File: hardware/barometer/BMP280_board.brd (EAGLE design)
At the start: 17.8 x 17.8 mm, 8 parts, among them U1 EM406FLAT

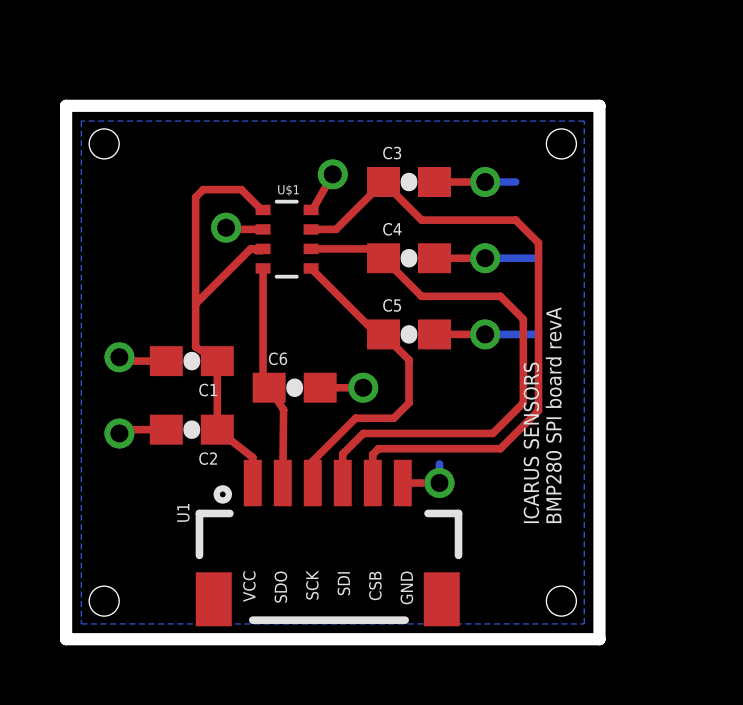
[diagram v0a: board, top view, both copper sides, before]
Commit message: schematic layout
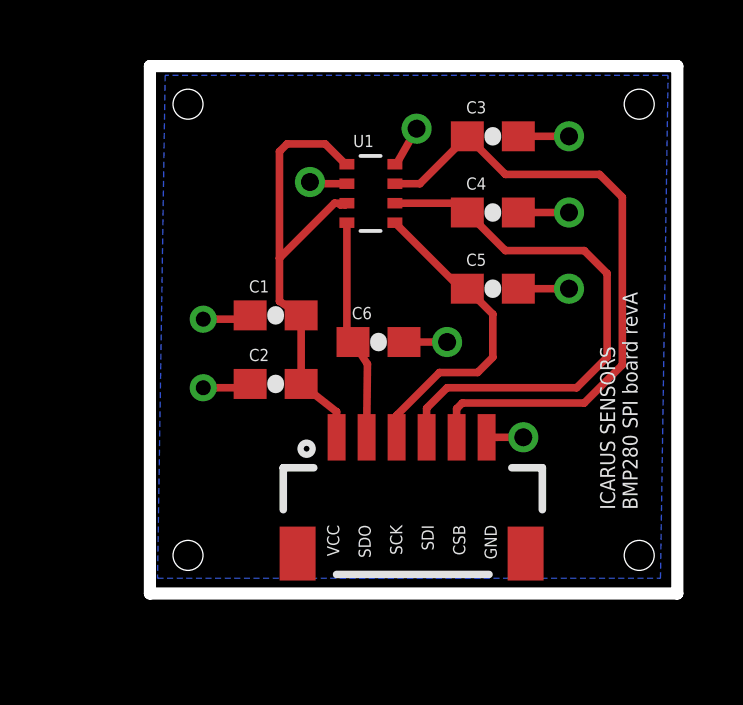
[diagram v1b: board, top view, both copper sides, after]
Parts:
- removed U$1: BMP280_PITCH0.65, icarus_sensors:LGA-8
- added U2: EM406FLAT, icarus_sensors:EM406-FLAT
- U1: value EM406FLAT -> BMP280; device icarus_sensors:EM406-FLAT -> icarus_sensors:LGA-8
- moved U1 12.7 mm to (7.62, 13.6)
- moved C1 3.18 mm to (4.45, 9.53)
- moved C2 3.18 mm to (4.45, 7.24)
- moved C4 3.18 mm to (11.7, 13.0)
- moved C3 3.18 mm to (11.7, 15.5)
- moved C5 3.18 mm to (11.7, 10.4)
- moved C6 3.18 mm to (7.87, 8.64)
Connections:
- net CSB: now also U1.2, U2.5; no longer U$1.2, U1.5
- net GND: now also U1.1, U1.7, U2.6; no longer U$1.1, U$1.7, U1.6
- net SCK: now also U1.4, U2.3; no longer U$1.4, U1.3
- net SDI: now also U1.3, U2.4; no longer U$1.3, U1.4
- net SDO: now also U1.5, U2.2; no longer U$1.5, U1.2
- net VCC: now also U1.6, U1.8, U2.1; no longer U$1.6, U$1.8, U1.1
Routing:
- net GND: track 20.6 -> 13.8 mm
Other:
- board size 17.8 x 17.8 mm -> 17.6 x 17.6 mm
